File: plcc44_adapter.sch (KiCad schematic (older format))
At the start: 4 parts, among them J1 Conn_01x20_Male, J2 Conn_01x20_Male, U1 ATmega8515-16JU, U2 PIC16F74-IP

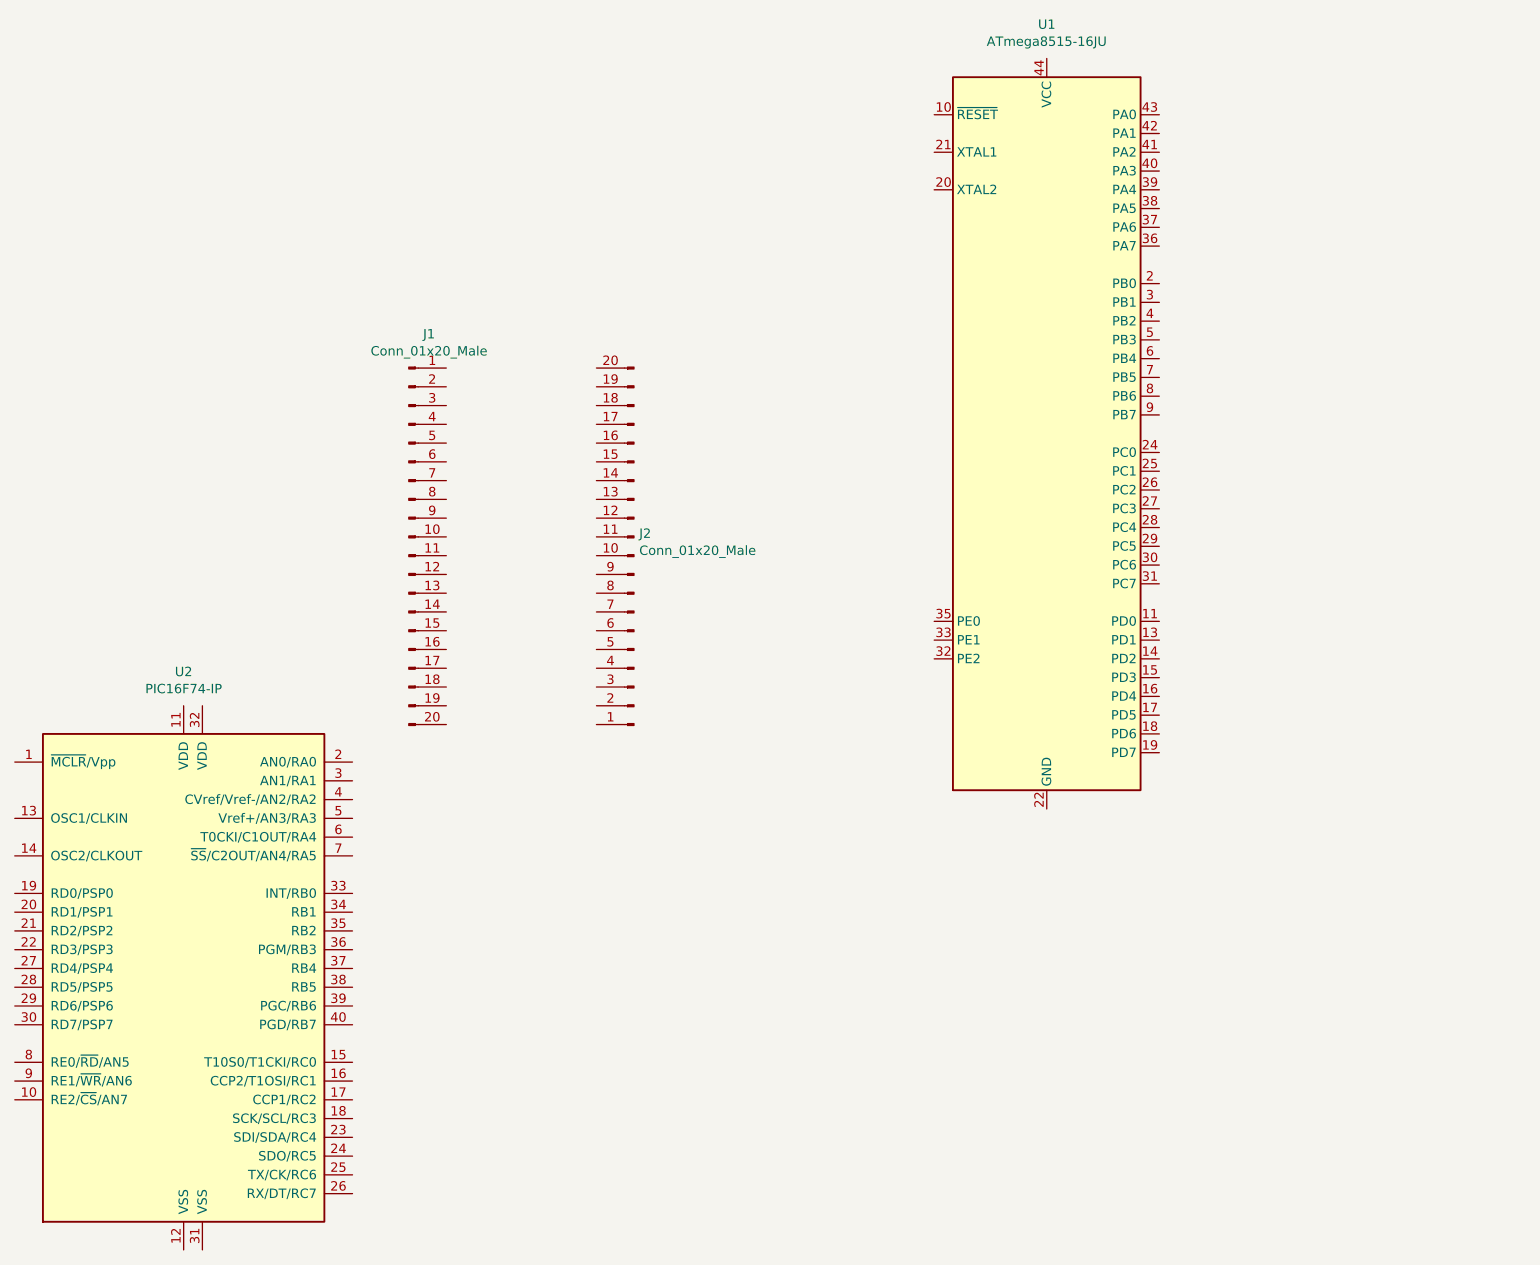
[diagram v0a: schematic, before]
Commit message: Added PLC44 Symbol
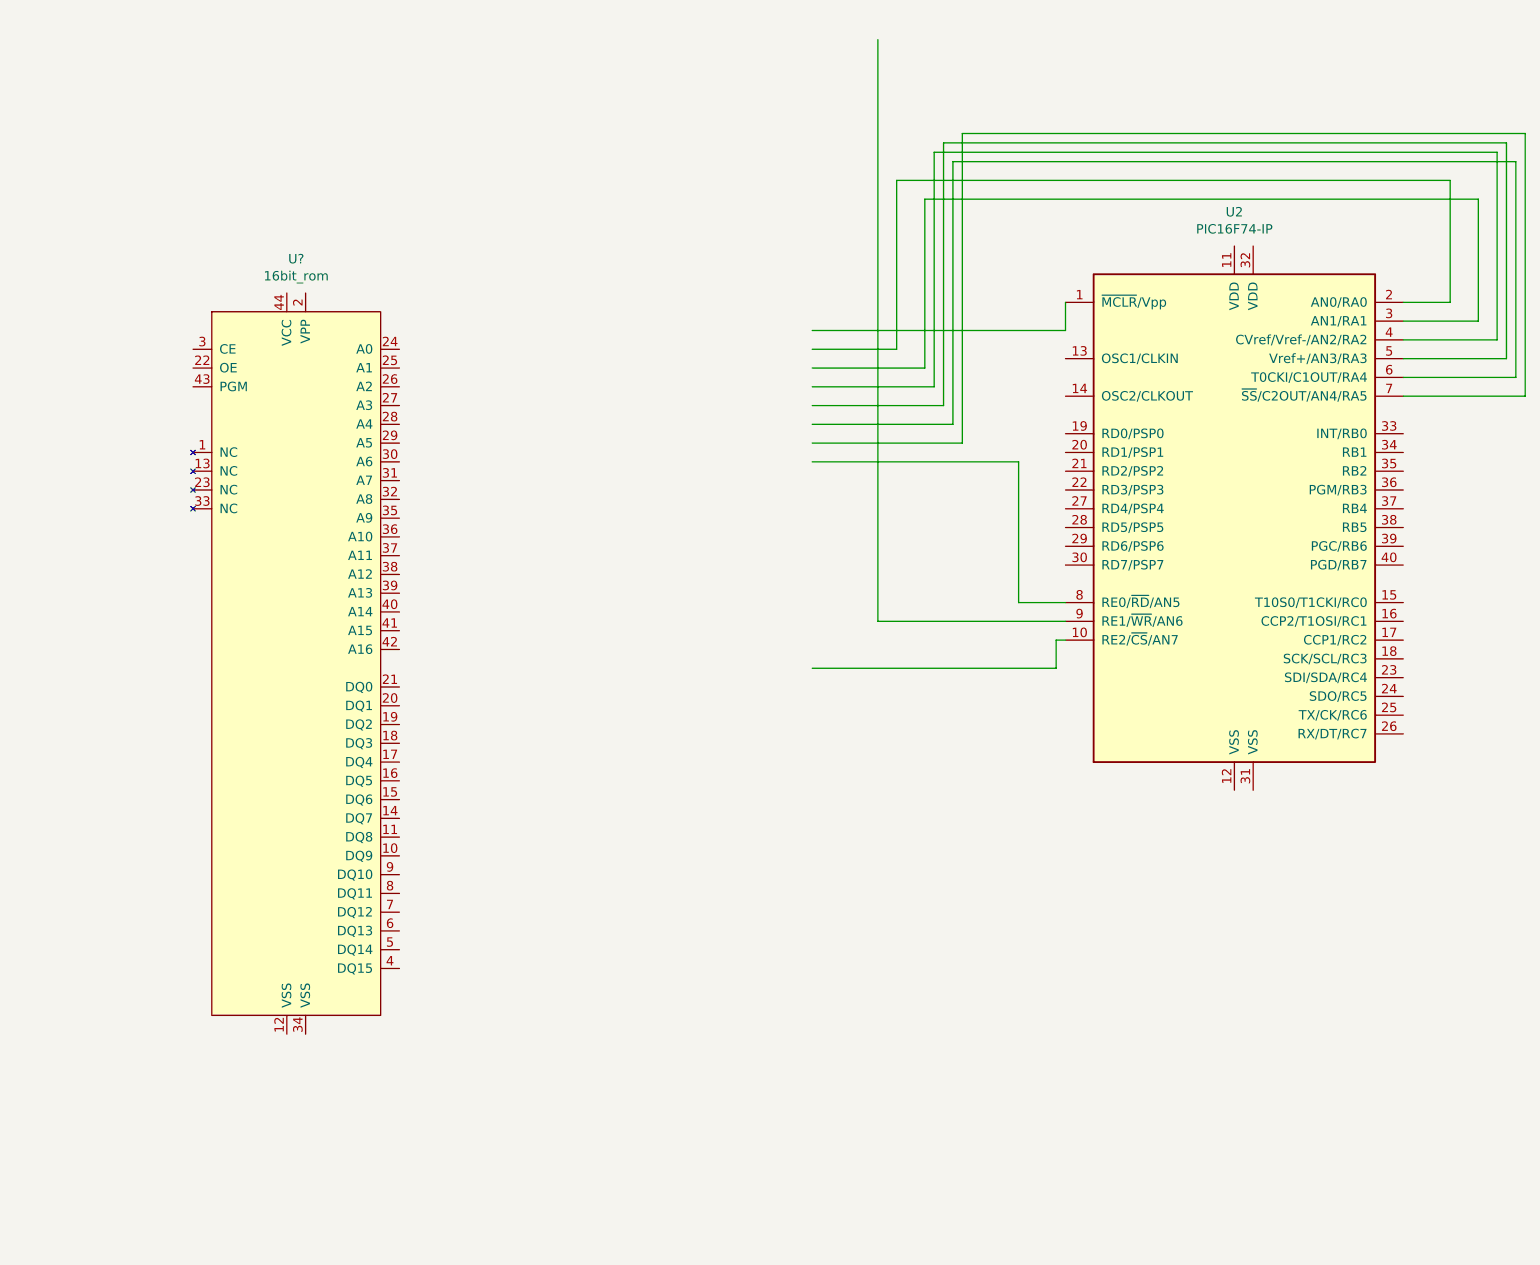
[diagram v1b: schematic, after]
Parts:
- removed J1, J2: Conn_01x20_Male, Connector_PinHeader_2.54mm:PinHeader_1x20_P2.54mm_Vertical, symbol Connector:Conn_01x20_Male
- removed U1: ATmega8515-16JU, Package_LCC:PLCC-44_THT-Socket, symbol MCU_Microchip_ATmega:ATmega8515-16JU
- added U?: 16bit_rom, symbol plcc44_16bitrom:16bit_rom
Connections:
- wire segments 0 -> 40
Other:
- moved on the sheet: U2
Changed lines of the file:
@@
 $EndDescr
-$Comp
-L Connector:Conn_01x20_Male J1
-U 1 1 5EA4DB18
-P 3450 3250
-F 0 "J1" H 3558 4331 50  0000 C CNN
-F 1 "Conn_01x20_Male" H 3558 4240 50  0000 C CNN
-F 2 "Connector_PinHeader_2.54mm:PinHeader_1x20_P2.54mm_Vertical" H 3450 3250 50  0001 C CNN
-F 3 "~" H 3450 3250 50  0001 C CNN
-	1    3450 3250
-	1    0    0    -1
-$EndComp
-$Comp
-L Connector:Conn_01x20_Male J2
-U 1 1 5EA4F830
-P 4650 3350
-F 0 "J2" H 4622 3232 50  0000 R CNN
-F 1 "Conn_01x20_Male" H 4622 3323 50  0000 R CNN
-F 2 "Connector_PinHeader_2.54mm:PinHeader_1x20_P2.54mm_Vertical" H 4650 3350 50  0001 C CNN
-F 3 "~" H 4650 3350 50  0001 C CNN
-	1    4650 3350
-	-1   0    0    1
-$EndComp
-$Comp
-L MCU_Microchip_ATmega:ATmega8515-16JU U1
-U 1 1 5EA534F9
-P 6850 2700
-F 0 "U1" H 6850 4881 50  0000 C CNN
-F 1 "ATmega8515-16JU" H 6850 4790 50  0000 C CNN
-F 2 "Package_LCC:PLCC-44_THT-Socket" H 6850 2700 50  0001 C CIN
-F 3 "http://ww1.microchip.com/downloads/en/DeviceDoc/doc2512.pdf" H 6850 2700 50  0001 C CNN
-	1    6850 2700
-	1    0    0    -1
-$EndComp
 $Comp
 L MCU_Microchip_PIC16:PIC16F74-IP U2
 U 1 1 5EA593D0
-P 2250 5550
-F 0 "U2" H 2250 7131 50  0000 C CNN
-F 1 "PIC16F74-IP" H 2250 7040 50  0000 C CNN
-F 2 "Package_DIP:DIP-40_W15.24mm" H 2250 5550 50  0001 C CIN
-F 3 "http://ww1.microchip.com/downloads/en/DeviceDoc/30325b.pdf" H 2250 5550 50  0001 C CNN
-	1    2250 5550
+P 7850 3100
+F 0 "U2" H 7850 4681 50  0000 C CNN
+F 1 "PIC16F74-IP" H 7850 4590 50  0000 C CNN
+F 2 "Package_DIP:DIP-40_W15.24mm" H 7850 3100 50  0001 C CIN
+F 3 "http://ww1.microchip.com/downloads/en/DeviceDoc/30325b.pdf" H 7850 3100 50  0001 C CNN
+	1    7850 3100
 	1    0    0    -1
 $EndComp
+Wire Wire Line
+	5600 2150 6950 2150
+Wire Wire Line
+	6950 2150 6950 2000
+Wire Wire Line
+	8750 2000 9000 2000
+Wire Wire Line
+	9000 2000 9000 1350
+Wire Wire Line
+	9000 1350 6050 1350
+Wire Wire Line
+	6050 1350 6050 2250
+Wire Wire Line
+	6050 2250 5600 2250
+Wire Wire Line
+	5600 2350 6200 2350
+Wire Wire Line
+	6200 2350 6200 1450
+Wire Wire Line
+	6200 1450 9150 1450
+Wire Wire Line
+	9150 1450 9150 2100
+Wire Wire Line
+	9150 2100 8750 2100
+Wire Wire Line
+	5600 2450 6250 2450
+Wire Wire Line
+	6250 2450 6250 1200
+Wire Wire Line
+	6250 1200 9250 1200
+Wire Wire Line
+	9250 1200 9250 2200
+Wire Wire Line
+	9250 2200 8750 2200
+Wire Wire Line
+	8750 2300 9300 2300
+Wire Wire Line
+	9300 2300 9300 1150
+Wire Wire Line
+	9300 1150 6300 1150
+Wire Wire Line
+	6300 1150 6300 2550
+Wire Wire Line
+	6300 2550 5600 2550
+Wire Wire Line
+	5600 2650 6350 2650
+Wire Wire Line
+	6350 2650 6350 1250
+Wire Wire Line
+	6350 1250 9350 1250
+Wire Wire Line
+	9350 1250 9350 2400
+Wire Wire Line
+	9350 2400 8750 2400
+Wire Wire Line
+	8750 2500 9400 2500
+Wire Wire Line
+	9400 2500 9400 1100
+Wire Wire Line
+	9400 1100 6400 1100
+Wire Wire Line
+	6400 1100 6400 2750
+Wire Wire Line
+	6400 2750 5600 2750
+Wire Wire Line
+	6950 3600 6700 3600
+Wire Wire Line
+	6700 3600 6700 2850
+Wire Wire Line
+	6700 2850 5600 2850
+Wire Wire Line
+	5950 600  5950 3700
+Wire Wire Line
+	5950 3700 6950 3700
+Wire Wire Line
+	6950 3800 6900 3800
+Wire Wire Line
+	6900 3800 6900 3950
+Wire Wire Line
+	6900 3950 5600 3950
+$Comp
+L plcc44_16bitrom:16bit_rom U?
+U 1 1 5EA76A43
+P 2850 3950
+F 0 "U?" H 2850 6131 50  0000 C CNN
+F 1 "16bit_rom" H 2850 6040 50  0000 C CNN
+F 2 "" H 2850 3950 50  0001 C CNN
+F 3 "" H 2850 3950 50  0001 C CNN
+	1    2850 3950
+	1    0    0    -1
+$EndComp

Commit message: Updated Symbols Updates Footprints for easier soldering
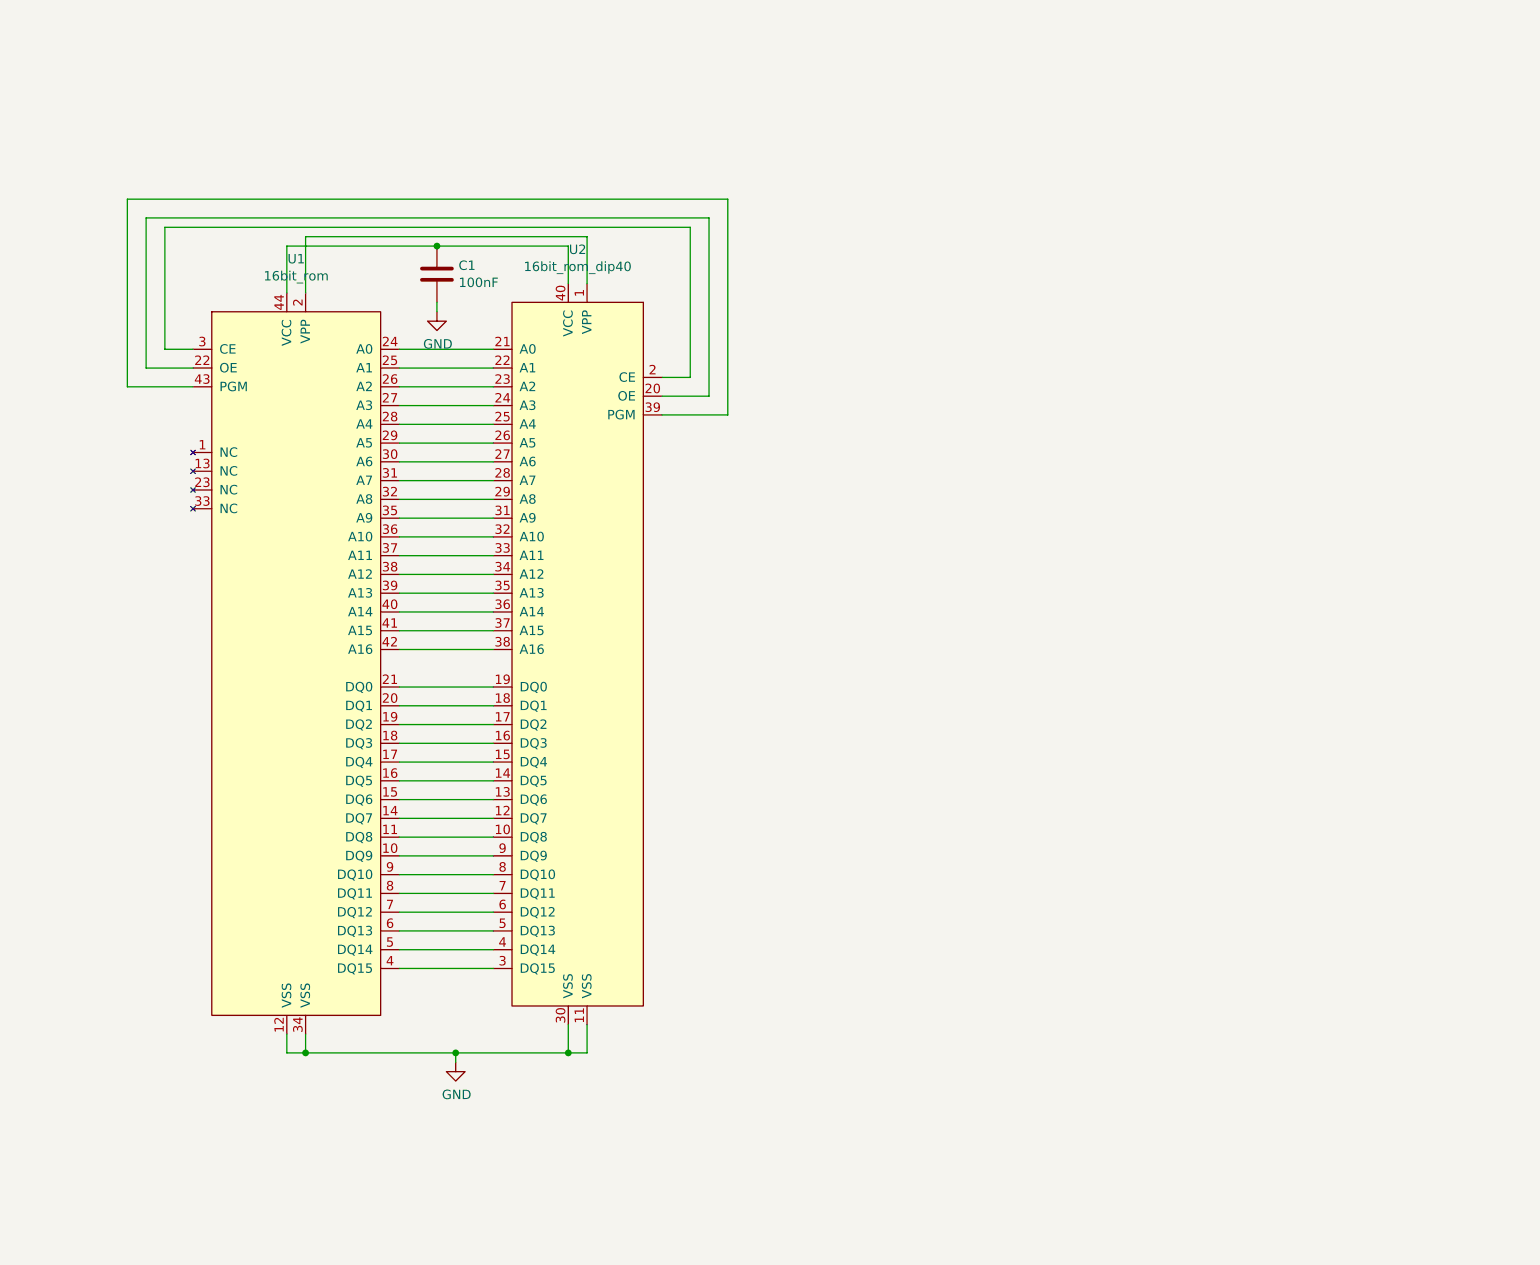
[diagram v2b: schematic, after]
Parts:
- removed U2: PIC16F74-IP, Package_DIP:DIP-40_W15.24mm, symbol MCU_Microchip_PIC16:PIC16F74-IP
- added C1: 100nF, Capacitor_SMD:C_0603_1608Metric, symbol Device:C
- added U2: 16bit_rom_dip40, dip40_mod:DIP-40_W15.24mm_mod, symbol plcc44_16bitrom:16bit_rom_dip40
- U1: renamed from U?; footprint (none) -> dip40_mod:PLCC-44_THT-Socket_mod
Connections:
- net labels added: GND
- wire segments 40 -> 65
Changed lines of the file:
@@
 $EndDescr
 $Comp
-L MCU_Microchip_PIC16:PIC16F74-IP U2
-U 1 1 5EA593D0
-P 7850 3100
-F 0 "U2" H 7850 4681 50  0000 C CNN
-F 1 "PIC16F74-IP" H 7850 4590 50  0000 C CNN
-F 2 "Package_DIP:DIP-40_W15.24mm" H 7850 3100 50  0001 C CIN
-F 3 "http://ww1.microchip.com/downloads/en/DeviceDoc/30325b.pdf" H 7850 3100 50  0001 C CNN
-	1    7850 3100
-	1    0    0    -1
-$EndComp
-Wire Wire Line
-	5600 2150 6950 2150
-Wire Wire Line
-	6950 2150 6950 2000
-Wire Wire Line
-	8750 2000 9000 2000
-Wire Wire Line
-	9000 2000 9000 1350
-Wire Wire Line
-	9000 1350 6050 1350
-Wire Wire Line
-	6050 1350 6050 2250
-Wire Wire Line
-	6050 2250 5600 2250
-Wire Wire Line
-	5600 2350 6200 2350
-Wire Wire Line
-	6200 2350 6200 1450
-Wire Wire Line
-	6200 1450 9150 1450
-Wire Wire Line
-	9150 1450 9150 2100
-Wire Wire Line
-	9150 2100 8750 2100
-Wire Wire Line
-	5600 2450 6250 2450
-Wire Wire Line
-	6250 2450 6250 1200
-Wire Wire Line
-	6250 1200 9250 1200
-Wire Wire Line
-	9250 1200 9250 2200
-Wire Wire Line
-	9250 2200 8750 2200
-Wire Wire Line
-	8750 2300 9300 2300
-Wire Wire Line
-	9300 2300 9300 1150
-Wire Wire Line
-	9300 1150 6300 1150
-Wire Wire Line
-	6300 1150 6300 2550
-Wire Wire Line
-	6300 2550 5600 2550
-Wire Wire Line
-	5600 2650 6350 2650
-Wire Wire Line
-	6350 2650 6350 1250
-Wire Wire Line
-	6350 1250 9350 1250
-Wire Wire Line
-	9350 1250 9350 2400
-Wire Wire Line
-	9350 2400 8750 2400
-Wire Wire Line
-	8750 2500 9400 2500
-Wire Wire Line
-	9400 2500 9400 1100
-Wire Wire Line
-	9400 1100 6400 1100
-Wire Wire Line
-	6400 1100 6400 2750
-Wire Wire Line
-	6400 2750 5600 2750
-Wire Wire Line
-	6950 3600 6700 3600
-Wire Wire Line
-	6700 3600 6700 2850
-Wire Wire Line
-	6700 2850 5600 2850
-Wire Wire Line
-	5950 600  5950 3700
-Wire Wire Line
-	5950 3700 6950 3700
-Wire Wire Line
-	6950 3800 6900 3800
-Wire Wire Line
-	6900 3800 6900 3950
-Wire Wire Line
-	6900 3950 5600 3950
-$Comp
-L plcc44_16bitrom:16bit_rom U?
+L plcc44_16bitrom:16bit_rom U1
 U 1 1 5EA76A43
 P 2850 3950
-F 0 "U?" H 2850 6131 50  0000 C CNN
+F 0 "U1" H 2850 6131 50  0000 C CNN
 F 1 "16bit_rom" H 2850 6040 50  0000 C CNN
-F 2 "" H 2850 3950 50  0001 C CNN
+F 2 "dip40_mod:PLCC-44_THT-Socket_mod" H 2850 3950 50  0001 C CNN
 F 3 "" H 2850 3950 50  0001 C CNN
 	1    2850 3950
 	1    0    0    -1
 $EndComp
+$Comp
+L plcc44_16bitrom:16bit_rom_dip40 U2
+U 1 1 5EA601FE
+P 4350 3950
+F 0 "U2" H 4350 6181 50  0000 C CNN
+F 1 "16bit_rom_dip40" H 4350 6090 50  0000 C CNN
+F 2 "dip40_mod:DIP-40_W15.24mm_mod" H 4350 3950 50  0001 C CNN
+F 3 "" H 4350 3950 50  0001 C CNN
+	1    4350 3950
+	-1   0    0    -1
+$EndComp
+Wire Wire Line
+	3400 2250 3900 2250
+Wire Wire Line
+	3400 2350 3900 2350
+Wire Wire Line
+	3400 2450 3900 2450
+Wire Wire Line
+	3400 2550 3900 2550
+Wire Wire Line
+	3400 2650 3900 2650
+Wire Wire Line
+	3400 2750 3900 2750
+Wire Wire Line
+	3400 2850 3900 2850
+Wire Wire Line
+	3400 2950 3900 2950
+Wire Wire Line
+	3400 3050 3900 3050
+Wire Wire Line
+	3400 3150 3900 3150
+Wire Wire Line
+	3400 3250 3900 3250
+Wire Wire Line
+	3400 3350 3900 3350
+Wire Wire Line
+	3400 3450 3900 3450
+Wire Wire Line
+	3400 3550 3900 3550
+Wire Wire Line
+	3400 3650 3900 3650
+Wire Wire Line
+	3400 3750 3900 3750
+Wire Wire Line
+	3400 3850 3900 3850
+Wire Wire Line
+	3400 4050 3900 4050
+Wire Wire Line
+	3400 4150 3900 4150
+Wire Wire Line
+	3400 4250 3900 4250
+Wire Wire Line
+	3400 4350 3900 4350
+Wire Wire Line
+	3400 4450 3900 4450
+Wire Wire Line
+	3900 4550 3400 4550
+Wire Wire Line
+	3400 4650 3900 4650
+Wire Wire Line
+	3400 4750 3900 4750
+Wire Wire Line
+	3400 4850 3900 4850
+Wire Wire Line
+	3400 4950 3900 4950
+Wire Wire Line
+	3400 5050 3900 5050
+Wire Wire Line
+	3400 5150 3900 5150
+Wire Wire Line
+	3400 5250 3900 5250
+Wire Wire Line
+	3400 5350 3900 5350
+Wire Wire Line
+	3400 5450 3900 5450
+Wire Wire Line
+	3400 5550 3900 5550
+Wire Wire Line
+	2900 1950 2900 1650
+Wire Wire Line
+	2900 1650 4400 1650
+Wire Wire Line
+	4400 1650 4400 1900
+Wire Wire Line
+	4300 1900 4300 1700
+Wire Wire Line
+	4300 1700 3600 1700
+Wire Wire Line
+	2800 1700 2800 1950
+$Comp
+L power:GND #PWR0101
+U 1 1 5EA6FAAC
+P 3700 6050
+F 0 "#PWR0101" H 3700 5800 50  0001 C CNN
+F 1 "GND" H 3705 5877 50  0000 C CNN
+F 2 "" H 3700 6050 50  0001 C CNN
+F 3 "" H 3700 6050 50  0001 C CNN
+	1    3700 6050
+	1    0    0    -1
+$EndComp
+Wire Wire Line
+	2800 5900 2800 6000
+Wire Wire Line
+	2800 6000 2900 6000
+Wire Wire Line
+	2900 5900 2900 6000
+Connection ~ 2900 6000
+Wire Wire Line
+	4300 6000 4300 5850
+Wire Wire Line
+	4400 5850 4400 6000
+Wire Wire Line
+	4400 6000 4300 6000
+Connection ~ 4300 6000
+Wire Wire Line
+	2900 6000 3700 6000
+Wire Wire Line
+	3700 6000 3700 6050
+Connection ~ 3700 6000
+Wire Wire Line
+	3700 6000 4300 6000
+Wire Wire Line
+	4800 2400 4950 2400
+Wire Wire Line
+	4950 2400 4950 1600
+Wire Wire Line
+	4950 1600 2150 1600
+Wire Wire Line
+	2150 1600 2150 2250
+Wire Wire Line
+	2150 2250 2300 2250
+Wire Wire Line
+	2300 2350 2050 2350
+Wire Wire Line
+	2050 2350 2050 1550
+Wire Wire Line
+	2050 1550 5050 1550
+Wire Wire Line
+	5050 1550 5050 2500
+Wire Wire Line
+	5050 2500 4800 2500
+Wire Wire Line
+	4800 2600 5150 2600
+Wire Wire Line
+	5150 2600 5150 1450
+Wire Wire Line
+	5150 1450 1950 1450
+Wire Wire Line
+	1950 1450 1950 2450
+Wire Wire Line
+	1950 2450 2300 2450
+$Comp
+L Device:C C1
+U 1 1 5EA7DCC0
+P 3600 1850
+F 0 "C1" H 3715 1896 50  0000 L CNN
+F 1 "100nF" H 3715 1805 50  0000 L CNN
+F 2 "Capacitor_SMD:C_0603_1608Metric" H 3638 1700 50  0001 C CNN
+F 3 "~" H 3600 1850 50  0001 C CNN
+	1    3600 1850
+	1    0    0    -1
+$EndComp
+Connection ~ 3600 1700
+Wire Wire Line
+	3600 1700 2800 1700
+$Comp
+L power:GND #PWR0102
+U 1 1 5EA7EDB4
+P 3600 2050
+F 0 "#PWR0102" H 3600 1800 50  0001 C CNN
+F 1 "GND" H 3605 1877 50  0000 C CNN
+F 2 "" H 3600 2050 50  0001 C CNN
+F 3 "" H 3600 2050 50  0001 C CNN
+	1    3600 2050
+	1    0    0    -1
+$EndComp
+Wire Wire Line
+	3600 2000 3600 2050
 $EndSCHEMATC
